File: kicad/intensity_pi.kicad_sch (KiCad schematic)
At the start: 68 parts, among them J1 Input A, J2 Input B / Setpoint, J3 Monitor, J4 Output, J7 select 1, SW1 SW_SPDT, SW2 SW_SPDT, SW3 SW_SPDT, SW5 EG6100-ND, U1 LM4040DBZ-5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

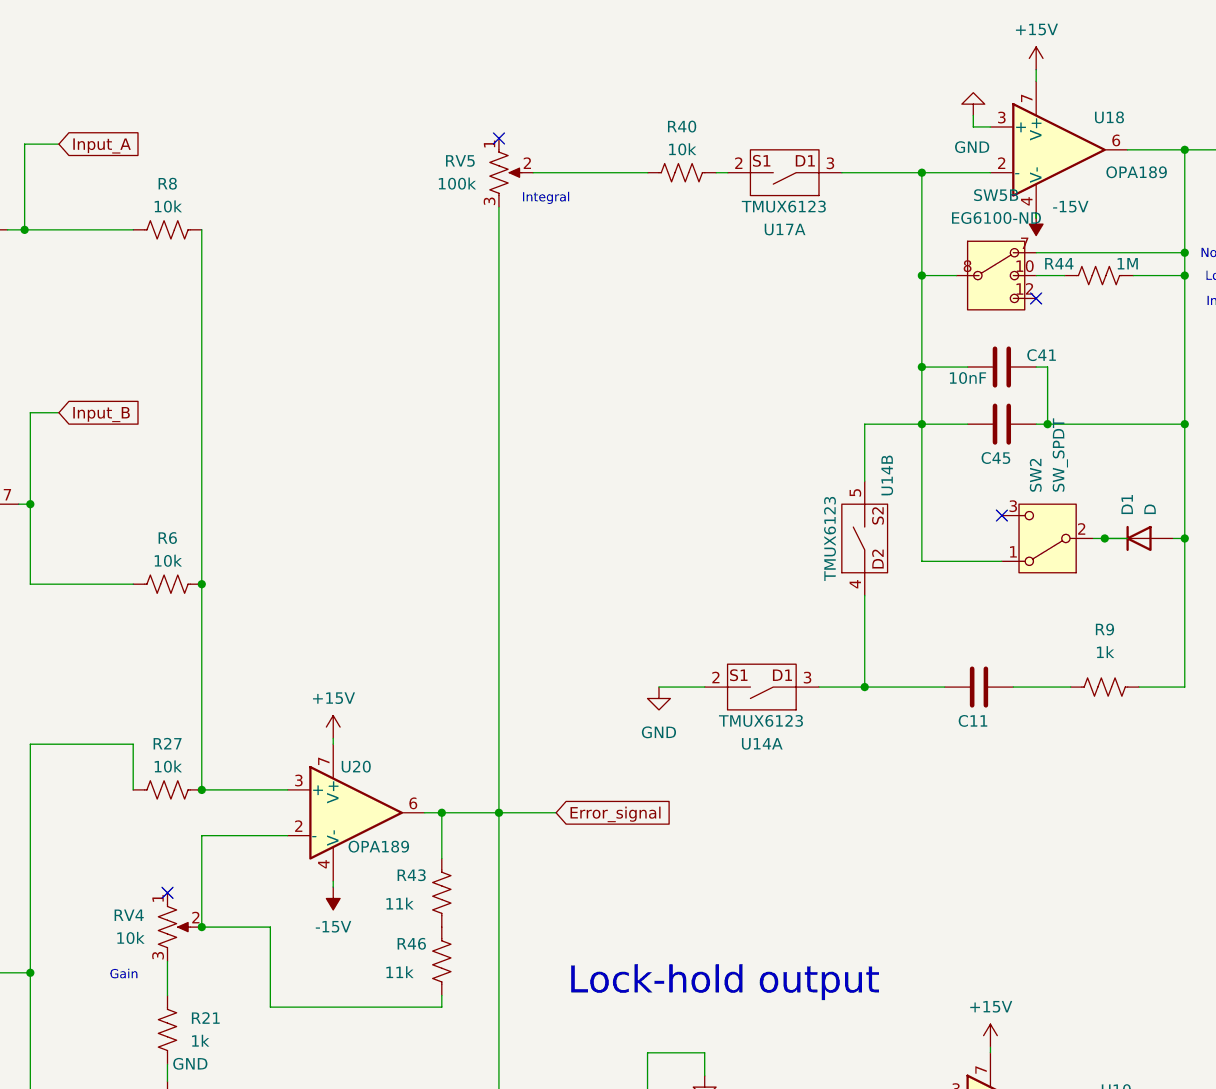
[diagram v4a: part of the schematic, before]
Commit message: Connected other leg of Pots, added 3d models from manufacturer for switch+pots
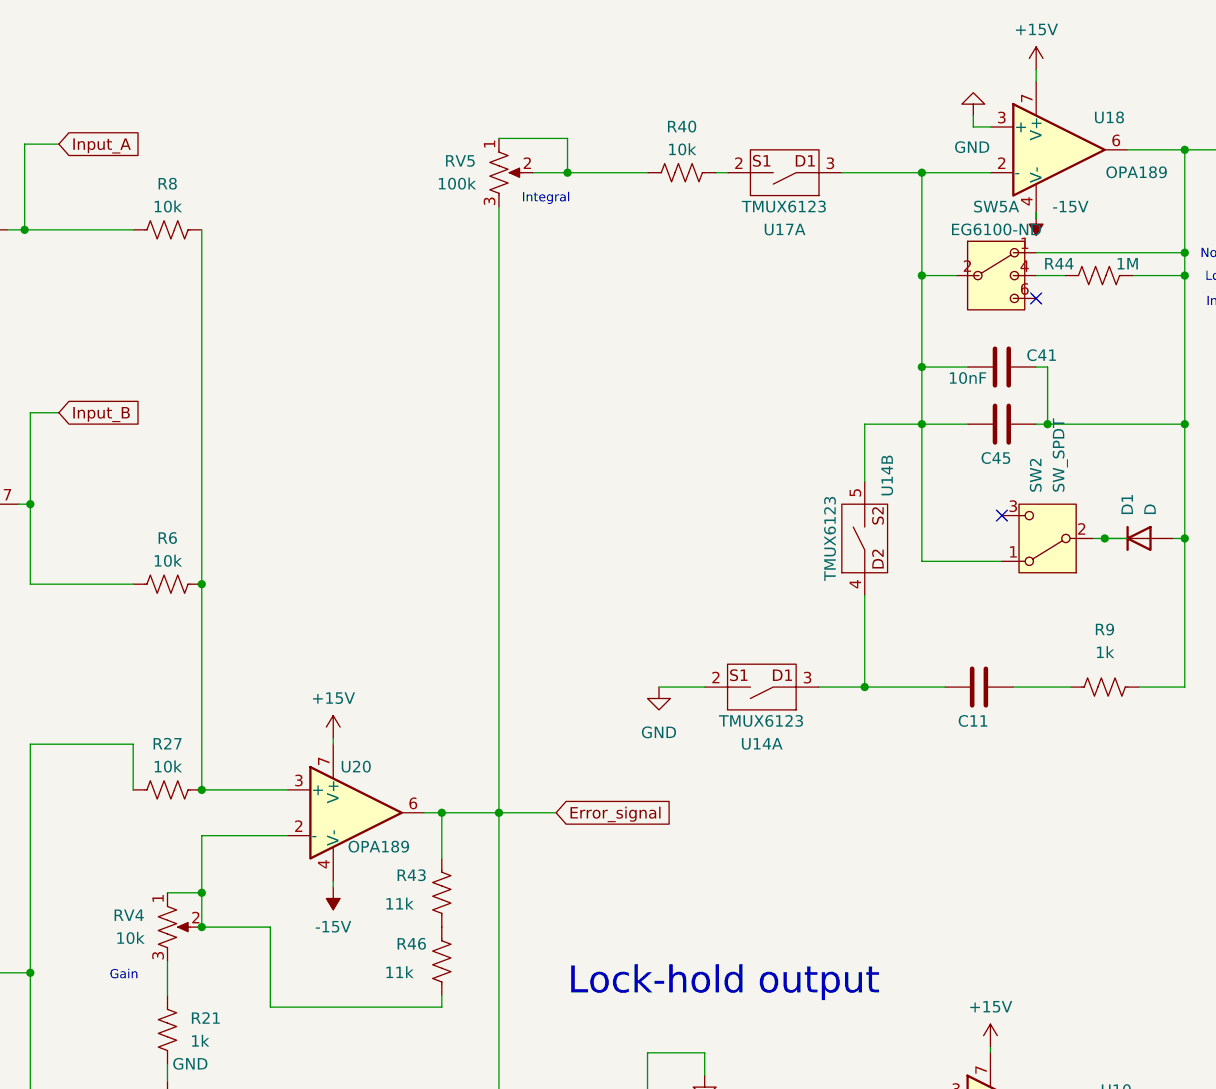
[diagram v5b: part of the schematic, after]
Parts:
- removed SW5: EG6100-ND, Custom_Footprints:Right Angle 3PDT Switch, symbol Custom_Symbols:DP3T_1
- added SW5: EG6100-ND, Custom_Footprints:Right Angle 3PDT Switch, symbol Custom_Symbols:DP3T_1
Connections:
- net at C41.1, C45.2, D1.2 (A)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: now also SW5.1
- net at C41.2, C45.1, SW2.1 (A)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: now also SW5.2
- net at R40.1, RV5.2: now also RV5.1
- net at RV4.1: now also R46.1, RV4.2, U20.2 (-)
- net at R44.1: now also SW5.4
- no-connect marks 6 -> 4
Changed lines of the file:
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@@
 	)
 	(junction
+		(at 91.44 110.49)
+		(diameter 0)
+		(color 0 0 0 0)
+	)
+	(junction
 		(at 25.4 39.37)
 		(diameter 0)
@@
 	)
 	(junction
+		(at 132.08 30.48)
+		(diameter 0)
+		(color 0 0 0 0)
+	)
+	(junction
 		(at 219.71 104.14)
 		(diameter 0)
@@
 	)
 	(no_connect
-		(at 124.46 26.67)
-	)
-	(no_connect
 		(at 232.41 129.54)
 	)
@@
 		(at 184.15 44.45)
 	)
-	(no_connect
-		(at 87.63 110.49)
-	)
 	(wire
 		(pts
@@
 	(wire
 		(pts
+			(xy 124.46 26.67) (xy 132.08 26.67)
+		)
+		(stroke
+			(width 0)
+			(type default)
+		)
+	)
+	(wire
+		(pts
 			(xy 45.72 116.84) (xy 46.99 116.84)
 		)
@@
 	(wire
 		(pts
-			(xy 91.44 104.14) (xy 91.44 114.3)
+			(xy 91.44 104.14) (xy 91.44 110.49)
 		)
 		(stroke
@@
 	(wire
 		(pts
+			(xy 132.08 26.67) (xy 132.08 30.48)
+		)
+		(stroke
+			(width 0)
+			(type default)
+		)
+	)
+	(wire
+		(pts
 			(xy 219.71 114.3) (xy 234.315 114.3)
 		)
@@
 	(wire
 		(pts
+			(xy 87.63 110.49) (xy 91.44 110.49)
+		)
+		(stroke
+			(width 0)
+			(type default)
+		)
+	)
+	(wire
+		(pts
 			(xy 180.34 73.66) (xy 171.45 73.66)
 		)
@@
 	(wire
 		(pts
-			(xy 128.27 30.48) (xy 140.97 30.48)
+			(xy 128.27 30.48) (xy 132.08 30.48)
 		)
 		(stroke
@@
 	(wire
 		(pts
+			(xy 91.44 110.49) (xy 91.44 114.3)
+		)
+		(stroke
+			(width 0)
+			(type default)
+		)
+	)
+	(wire
+		(pts
 			(xy 15.24 115.57) (xy 19.05 115.57)
 		)
@@
 	(wire
 		(pts
+			(xy 132.08 30.48) (xy 140.97 30.48)
+		)
+		(stroke
+			(width 0)
+			(type default)
+		)
+	)
+	(wire
+		(pts
 			(xy 19.05 115.57) (xy 19.05 121.92)
 		)
@@
 	)
 	(symbol
+		(lib_id "Custom_Symbols:DP3T_1")
+		(at 179.07 41.91 0)
+		(unit 1)
+		(exclude_from_sim no)
+		(in_bom yes)
+		(on_board yes)
+		(dnp no)
+		(property "Reference" "SW5"
+			(at 179.705 34.29 0)
+			(effects
+				(font
+					(size 1.27 1.27)
+				)
+			)
+		)
+		(property "Value" "EG6100-ND"
+			(at 179.705 36.83 0)
+			(effects
+				(font
+					(size 1.27 1.27)
+				)
+			)
+		)
+		(property "Footprint" "Custom_Footprints:Right Angle 3PDT Switch"
+			(at 179.07 41.91 0)
+			(effects
+				(font
+					(size 1.27 1.27)
+				)
+				(hide yes)
+			)
+		)
+		(property "Datasheet" ""
+			(at 179.07 41.91 0)
+			(effects
+				(font
+					(size 1.27 1.27)
+				)
+				(hide yes)
+			)
+		)
+		(property "Description" ""
+			(at 179.07 41.91 0)
+			(effects
+				(font
+					(size 1.27 1.27)
+				)
+				(hide yes)
+			)
+		)
+		(property "DIGIKEY" "EG6100-ND"
+			(at 179.07 41.91 0)
+			(effects
+				(font
+					(size 1.27 1.27)
+				)
+				(hide yes)
+			)
+		)
+		(property "PARTNO" "1004P6T1B4M7RE"
+			(at 179.07 41.91 0)
+			(effects
+				(font
+					(size 1.27 1.27)
+				)
+				(hide yes)
+			)
+		)
+		(property "MPN" ""
+			(at 179.07 41.91 0)
+			(effects
+				(font
+					(size 1.27 1.27)
+				)
+				(hide yes)
+			)
+		)
+		(pin "9"
+		)
+		(pin "10"
+		)
+		(pin "3"
+		)
+		(pin "5"
+		)
+		(pin "12"
+		)
+		(pin "8"
+		)
+		(pin "11"
+		)
+		(pin "7"
+		)
+		(pin "13"
+		)
+		(pin "6"
+		)
+		(pin "2"
+		)
+		(pin "4"
+		)
+		(pin "1"
+		)
+		(instances
+			(project "intensity_pi"
+				(path "/3a3d7bcb-6fa5-41ef-9ea1-6d4ab7c492fd"
+					(reference "SW5")
+					(unit 1)
+				)
+			)
+		)
+	)
+	(symbol
 		(lib_id "Device:R_US")
 		(at 181.61 160.02 90)
@@
 					(unit 2)
 				)
-			)
-		)
-	)
-	(symbol
-		(lib_id "Custom_Symbols:DP3T_1")
-		(at 179.07 41.91 0)
-		(unit 2)
-		(exclude_from_sim no)
-		(in_bom yes)
-		(on_board yes)
-		(dnp no)
-		(fields_autoplaced yes)
-		(property "Reference" "SW5"
-			(at 179.705 33.02 0)
-			(effects
-				(font
-					(size 1.27 1.27)
-				)
-			)
-		)
-		(property "Value" "EG6100-ND"
-			(at 179.705 35.56 0)
-			(effects
-				(font
-					(size 1.27 1.27)
-				)
-			)
-		)
-		(property "Footprint" "Custom_Footprints:Right Angle 3PDT Switch"
-			(at 179.07 41.91 0)
-			(effects
-				(font
-					(size 1.27 1.27)
-				)
-				(hide yes)
-			)
-		)
-		(property "Datasheet" ""
-			(at 179.07 41.91 0)
-			(effects
-				(font
-					(size 1.27 1.27)
-				)
-				(hide yes)
-			)
-		)
-		(property "Description" ""
-			(at 179.07 41.91 0)
-			(effects
-				(font
-					(size 1.27 1.27)
-				)
-				(hide yes)
-			)
-		)
-		(property "DIGIKEY" "EG6100-ND"
-			(at 179.07 41.91 0)
-			(effects
-				(font
-					(size 1.27 1.27)
-				)
-				(hide yes)
-			)
-		)
-		(property "PARTNO" "1004P6T1B4M7RE"
-			(at 179.07 41.91 0)
-			(effects
-				(font
-					(size 1.27 1.27)
-				)
-				(hide yes)
-			)
-		)
-		(property "MPN" ""
-			(at 179.07 41.91 0)
-			(effects
-				(font
-					(size 1.27 1.27)
-				)
-				(hide yes)
-			)
-		)
-		(pin "9"
-		)
-		(pin "10"
-		)
-		(pin "3"
-		)
-		(pin "5"
-		)
-		(pin "12"
-		)
-		(pin "8"
-		)
-		(pin "11"
-		)
-		(pin "7"
-		)
-		(pin "13"
-		)
-		(pin "6"
-		)
-		(pin "2"
-		)
-		(pin "4"
-		)
-		(pin "1"
-		)
-		(instances
-			(project "intensity_pi"
-				(path "/3a3d7bcb-6fa5-41ef-9ea1-6d4ab7c492fd"
-					(reference "SW5")
-					(unit 2)
-				)

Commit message: Fixed Digikey Part numbers for some parts, confirmed final BOM, Fixed Switch Footprint hole size
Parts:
- C1, C10: DIGIKEY 1276-6840-2-ND -> 1276-6840-1-ND
- C12: DIGIKEY 399-C0805C101J5GACTUTR-ND -> 399-C0805C101J5GACTUCT-ND
- C41: DIGIKEY 399-C0805C103K5RACTUTR-ND -> 399-C0805C103K5RACTUCT-ND
- D1, D2: DIGIKEY 4004-SSTPAD5SOT-233LROHSTR-ND -> 4004-SSTPAD5SOT-233LROHSCT-ND
- R13: DIGIKEY 118-CRT0805-BY-5001EASTR-ND -> 118-CRT0805-BY-5001EASCT-ND
- R15, R23: DIGIKEY 541-CRCW080550R0FKTATR-ND -> 541-CRCW080550R0FKTACT-ND
- R16: DIGIKEY P100KDATR-ND -> P100KDACT-ND
- R17, R21, R24, R26, R41, R9: DIGIKEY 5831-2-2176327-5TR-ND -> RG20P1.0KBCT-ND; PARTNO 2-2176327-5 -> RG2012P-102-B-T5
- R35, R36: DIGIKEY 311-3.30KCRTR-ND -> 311-3.30KCRCT-ND
- R37: DIGIKEY YAG3766CT-ND -> CR0805-FX-1800ELFCT-ND; PARTNO AC0805JR-071ML -> CR0805-FX-1800ELF
- R43, R46: DIGIKEY A126334TR-ND -> A126334CT-ND
- SW2, SW3: DIGIKEY CKN10546TR-ND -> CKN10546CT-ND
- U3, U4: DIGIKEY 296-INA849DRCT-ND‎ -> 296-INA849DRCT-ND
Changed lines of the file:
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@@
 			)
 		)
-		(property "DIGIKEY" "296-INA849DRCT-ND‎ "
+		(property "DIGIKEY" "296-INA849DRCT-ND"
 			(at 59.69 36.83 0)
 			(effects
@@
 			)
 		)
-		(property "DIGIKEY" "4004-SSTPAD5SOT-233LROHSTR-ND"
+		(property "DIGIKEY" "4004-SSTPAD5SOT-233LROHSCT-ND"
 			(at 195.58 71.12 0)
 			(effects
@@
 			)
 		)
-		(property "DIGIKEY" "1276-6840-2-ND "
+		(property "DIGIKEY" "1276-6840-1-ND "
 			(at 62.23 142.24 90)
 			(effects
@@
 			)
 		)
-		(property "DIGIKEY" "541-CRCW080550R0FKTATR-ND"
+		(property "DIGIKEY" "541-CRCW080550R0FKTACT-ND"
 			(at 267.97 80.01 90)
 			(effects
@@
 			)
 		)
-		(property "DIGIKEY" "118-CRT0805-BY-5001EASTR-ND"
+		(property "DIGIKEY" "118-CRT0805-BY-5001EASCT-ND"
 			(at 151.13 142.24 0)
 			(effects
@@
 			)
 		)
-		(property "DIGIKEY" "P100KDATR-ND"
+		(property "DIGIKEY" "P100KDACT-ND"
 			(at 181.61 160.02 0)
 			(effects
@@
 			)
 		)
-		(property "DIGIKEY" "5831-2-2176327-5TR-ND"
+		(property "DIGIKEY" "RG20P1.0KBCT-ND"
 			(at 191.77 87.63 0)
 			(effects
@@
 			)
 		)
-		(property "PARTNO" "2-2176327-5"
+		(property "PARTNO" "RG2012P-102-B-T5"
 			(at 191.77 87.63 90)
 			(effects
@@
 			)
 		)
-		(property "DIGIKEY" "399-C0805C103K5RACTUTR-ND"
+		(property "DIGIKEY" "399-C0805C103K5RACTUCT-ND"
 			(at 180.34 52.07 90)
 			(effects
@@
 			)
 		)
-		(property "DIGIKEY" "4004-SSTPAD5SOT-233LROHSTR-ND"
+		(property "DIGIKEY" "4004-SSTPAD5SOT-233LROHSCT-ND"
 			(at 250.19 132.08 0)
 			(effects
@@
 			)
 		)
-		(property "DIGIKEY" "A126334TR-ND"
+		(property "DIGIKEY" "A126334CT-ND"
 			(at 118.11 110.49 0)
 			(effects
@@
 			)
 		)
-		(property "DIGIKEY" "1276-6840-2-ND "
+		(property "DIGIKEY" "1276-6840-1-ND "
 			(at 37.465 123.19 90)
 			(effects
@@
 			)
 		)
-		(property "DIGIKEY" "5831-2-2176327-5TR-ND"
+		(property "DIGIKEY" "RG20P1.0KBCT-ND"
 			(at 87.63 125.73 0)
 			(effects
@@
 			)
 		)
-		(property "PARTNO" "2-2176327-5"
+		(property "PARTNO" "RG2012P-102-B-T5"
 			(at 87.63 125.73 0)
 			(effects
@@
 			)
 		)
-		(property "DIGIKEY" "296-INA849DRCT-ND‎ "
+		(property "DIGIKEY" "296-INA849DRCT-ND"
 			(at 60.96 67.31 0)
 			(effects
@@
 			)
 		)
-		(property "DIGIKEY" "CKN10546TR-ND"
+		(property "DIGIKEY" "CKN10546CT-ND"
 			(at 237.49 132.08 90)
 			(effects
@@
 			)
 		)
-		(property "DIGIKEY" "541-CRCW080550R0FKTATR-ND"
+		(property "DIGIKEY" "541-CRCW080550R0FKTACT-ND"
 			(at 162.56 181.61 90)
 			(effects
@@
 			)
 		)
-		(property "DIGIKEY" "CKN10546TR-ND"
+		(property "DIGIKEY" "CKN10546CT-ND"
 			(at 185.42 71.12 90)
 			(effects
@@
 			)
 		)
-		(property "DIGIKEY" "5831-2-2176327-5TR-ND"
+		(property "DIGIKEY" "RG20P1.0KBCT-ND"
 			(at 59.69 170.18 0)
 			(effects
@@
 			)
 		)
-		(property "PARTNO" "2-2176327-5"
+		(property "PARTNO" "RG2012P-102-B-T5"
 			(at 59.69 170.18 90)
 			(effects
@@
 			)
 		)
-		(property "DIGIKEY" "399-C0805C101J5GACTUTR-ND"
+		(property "DIGIKEY" "399-C0805C101J5GACTUCT-ND"
 			(at 238.125 114.3 90)
 			(effects
@@
 			)
 		)
-		(property "DIGIKEY" "YAG3766CT-ND"
+		(property "DIGIKEY" "CR0805-FX-1800ELFCT-ND"
 			(at 33.02 177.8 90)
 			(effects
@@
 			)
 		)
-		(property "PARTNO" "AC0805JR-071ML"
+		(property "PARTNO" "CR0805-FX-1800ELF"
 			(at 33.02 177.8 90)
 			(effects
@@
 			)
 		)
-		(property "DIGIKEY" "311-3.30KCRTR-ND"
+		(property "DIGIKEY" "311-3.30KCRCT-ND"
 			(at 252.73 93.98 0)
 			(effects
@@
 			)
 		)
-		(property "DIGIKEY" "5831-2-2176327-5TR-ND"
+		(property "DIGIKEY" "RG20P1.0KBCT-ND"
 			(at 25.4 73.66 0)
 			(effects
@@
 			)
 		)
-		(property "PARTNO" "2-2176327-5"
+		(property "PARTNO" "RG2012P-102-B-T5"
 			(at 25.4 73.66 0)
 			(effects
@@
 			)
 		)
-		(property "DIGIKEY" "311-3.30KCRTR-ND"
+		(property "DIGIKEY" "311-3.30KCRCT-ND"
 			(at 152.4 189.23 0)
 			(effects
@@
 			)
 		)
-		(property "DIGIKEY" "5831-2-2176327-5TR-ND"
+		(property "DIGIKEY" "RG20P1.0KBCT-ND"
 			(at 25.4 43.18 0)
 			(effects
@@
 			)
 		)
-		(property "PARTNO" "2-2176327-5"
+		(property "PARTNO" "RG2012P-102-B-T5"
 			(at 25.4 43.18 0)
 			(effects
@@
 			)
 		)
-		(property "DIGIKEY" "5831-2-2176327-5TR-ND"
+		(property "DIGIKEY" "RG20P1.0KBCT-ND"
 			(at 114.3 179.07 0)
 			(effects
@@
 			)
 		)
-		(property "PARTNO" "2-2176327-5"
+		(property "PARTNO" "RG2012P-102-B-T5"
 			(at 114.3 179.07 90)
 			(effects
@@
 			)
 		)
-		(property "DIGIKEY" "A126334TR-ND"
+		(property "DIGIKEY" "A126334CT-ND"
 			(at 118.11 118.11 0)
 			(effects
